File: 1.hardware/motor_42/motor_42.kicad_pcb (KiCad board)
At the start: 4 copper layers, 40 x 40 mm, 93 parts, among them IC1 TB67H450FNG,EL, IC2 TB67H450FNG,EL, J1 PC_CONN, J2 MT6816_CONN, J4 DEBUG, J5 CAN_IN, J6 CAN_OUT, J7 ESP_DOWNLOAD, J8 BOOT_EN, U1 TPS54202DDC, U2 STM32F103CBTx, U3 SN65HVD232, U4 TL431AIDBZR, U5 MT6816CT, U6 ESP32-C3-WROOM-02, Y1 YSX321SL_12Mhz

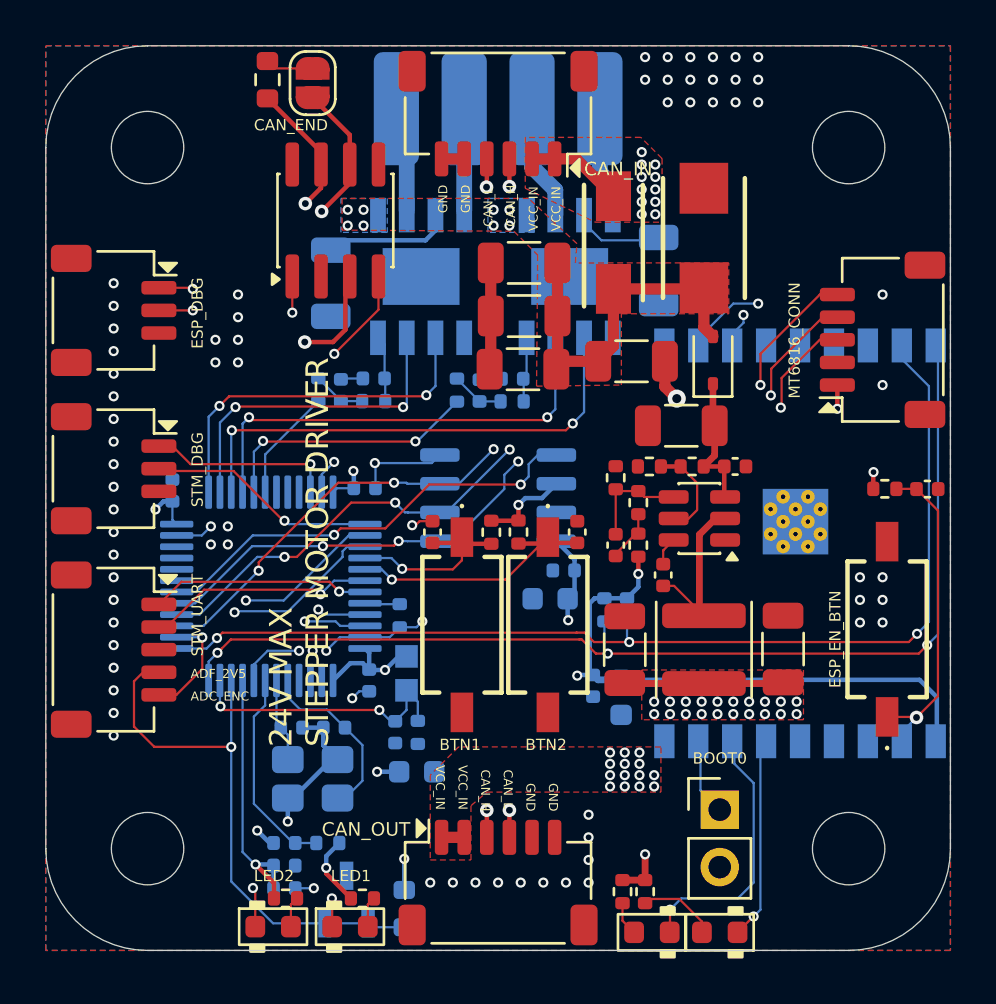
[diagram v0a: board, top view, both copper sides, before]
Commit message: 비아 변경 필요
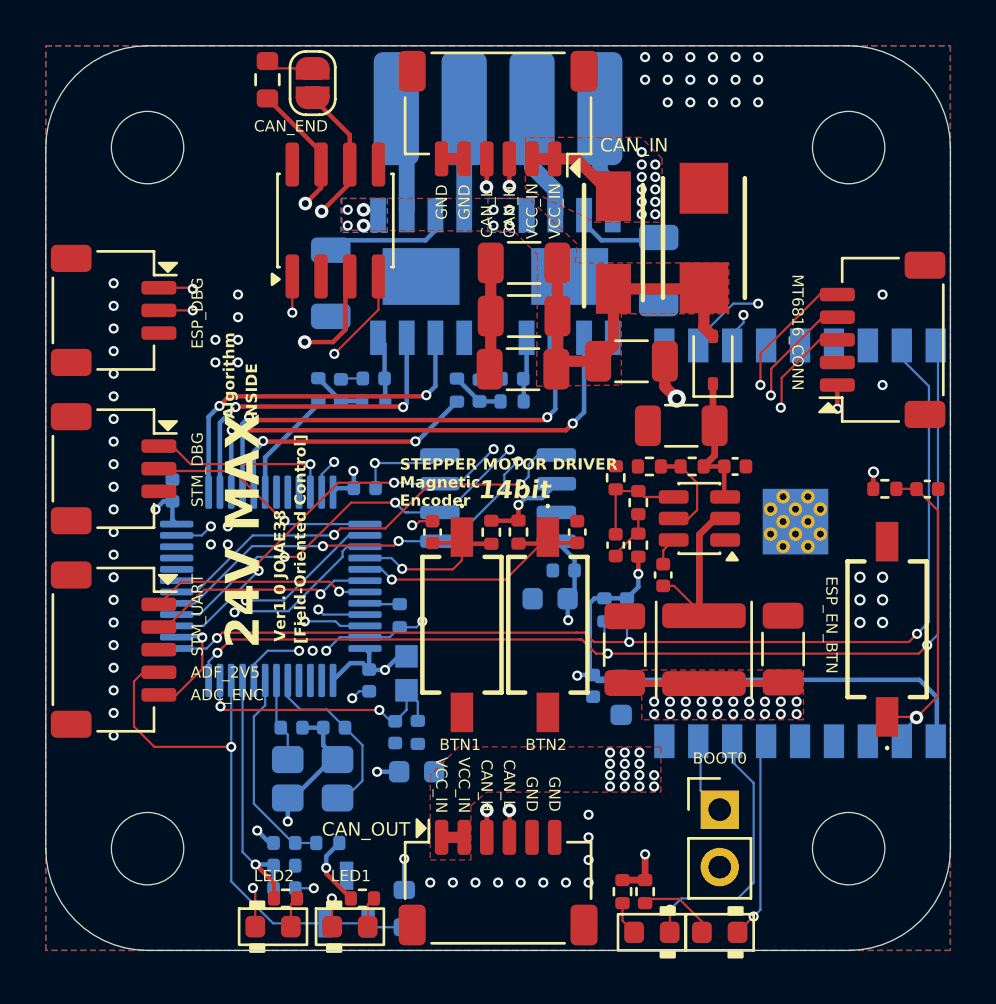
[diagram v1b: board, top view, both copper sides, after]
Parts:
- C15, C19, C31, C32: value 0.1uF/16V -> 0.1uF/50V
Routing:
- net Net-(IC1-RS): track 3.62 -> 4.12 mm
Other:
- board text added: "14bit"
- board text added: "24V MAX"
- board text added: "A-A+"
- board text added: "Algorithm"
- board text added: "B-B+"
- board text added: "INSIDE"
- board text added: "Magnetic Encoder"
- board text added: "STEPPER MOTOR DRIVER"
- board text added: "Ver1.0 JOJAE38"
- board text added: "[Field-Oriented Control]"
- board text removed: "24V MAX STEPPER MOTOR DRIVER"
- board text removed: "A+A-"
- board text removed: "B+B-"

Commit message: via 홀 0.3 직경 0.6(1.5의 폭 을 가진다) 수정 및 라우팅 개선
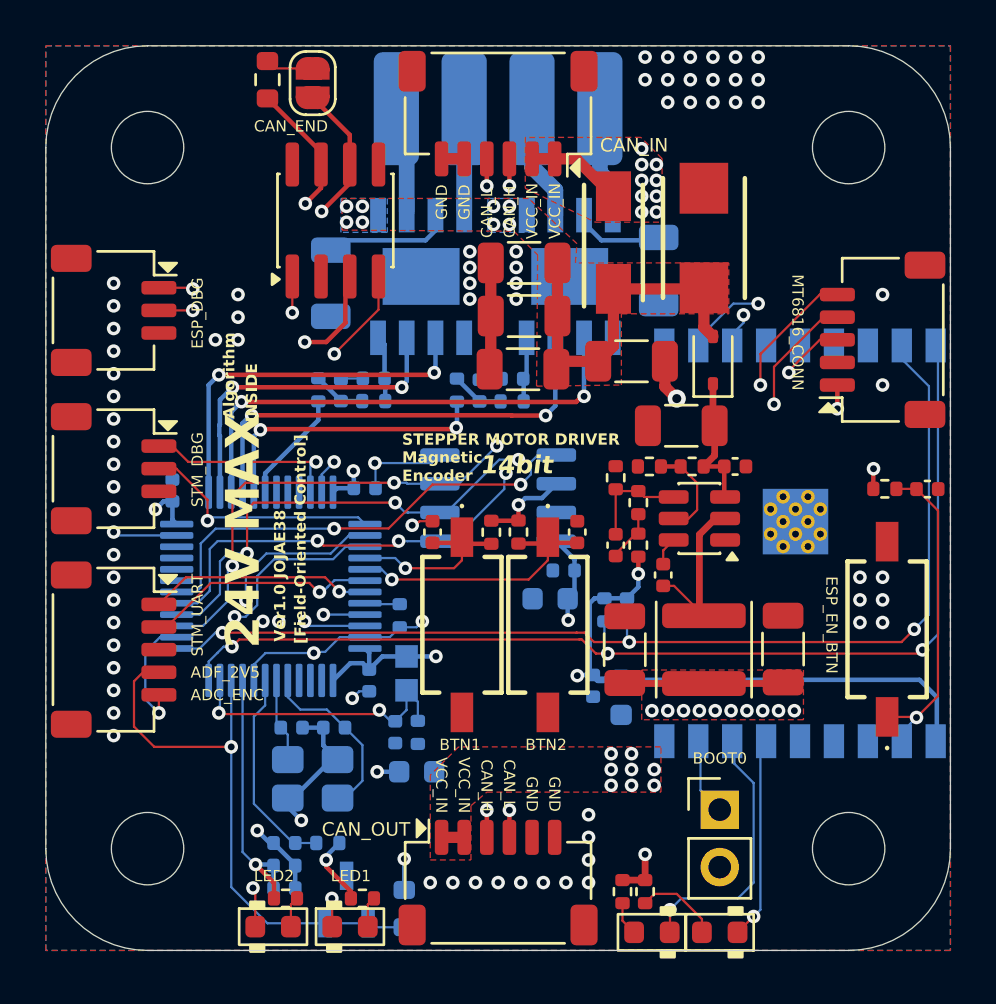
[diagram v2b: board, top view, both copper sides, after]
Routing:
- net GND: track 34.9 -> 39.1 mm, vias 79 -> 80
- net SPI1_MOSI: track 35.5 -> 37.7 mm
- net SPI1_MISO: track 36.3 -> 38.2 mm
- net 3V3: track 75.0 -> 76.2 mm, vias 35 -> 25
- net MT6816_CSN: track 19.6 -> 20.8 mm
- net VREF_PWM_A: track 11.8 -> 12.8 mm
- net SPI1_CLK: track 36.4 -> 37.3 mm
- net SWCLK: track 10.1 -> 10.9 mm
- net LED1: track 22.5 -> 23.1 mm
- net BTN2: track 11.9 -> 12.5 mm
- net LED2: track 21.4 -> 22.0 mm
- net VCC_IN: vias 25 -> 17
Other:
- board text added: "MT6816"
- board text removed: "MT6816_MAGNETIC"

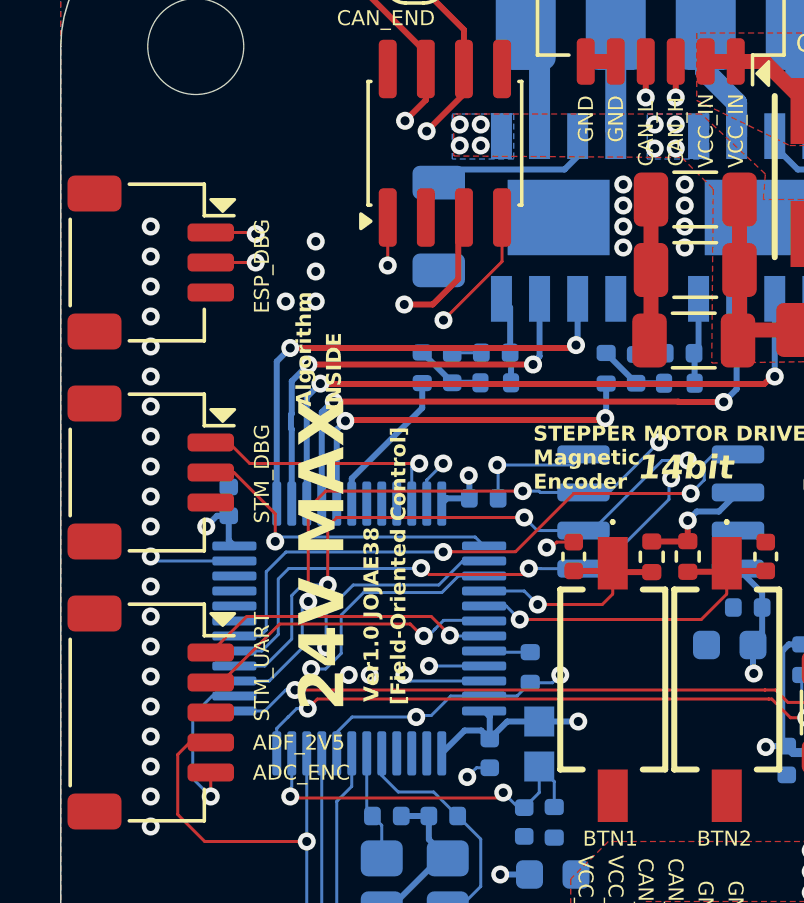
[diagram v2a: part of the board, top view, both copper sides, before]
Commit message: wifi ble 문양 추가
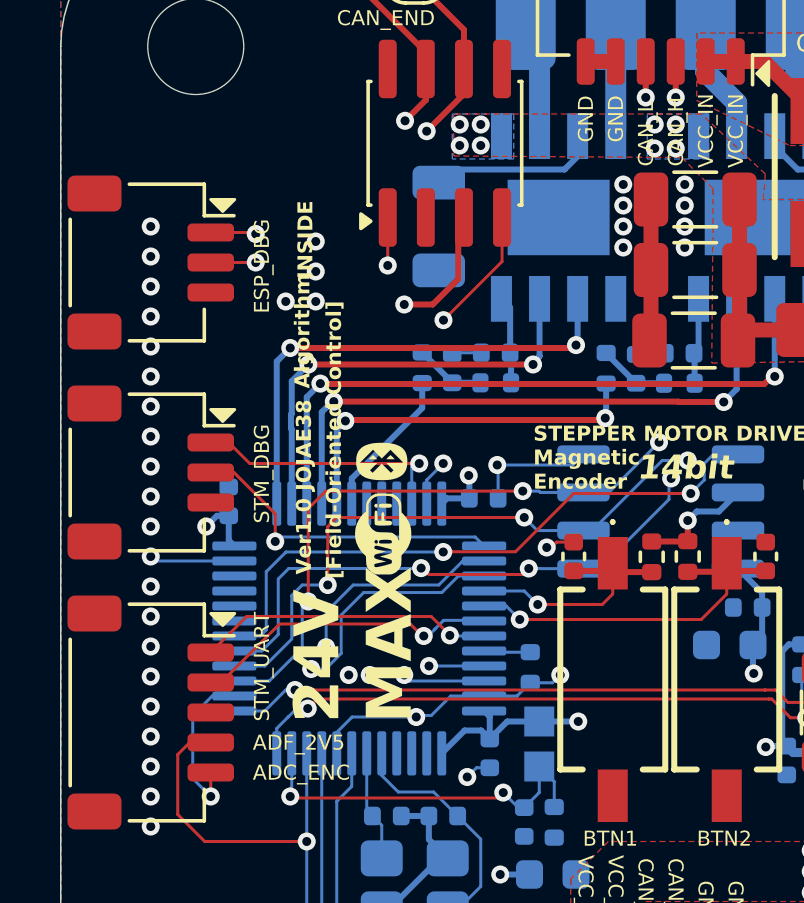
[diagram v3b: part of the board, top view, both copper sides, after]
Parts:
- added G***: LOGO, stepper_motor_controller:wifi, F.Cu at (61.8, 70.8)
- added G***: LOGO, stepper_motor_controller:ble, F.Cu at (61.7, 68.3)

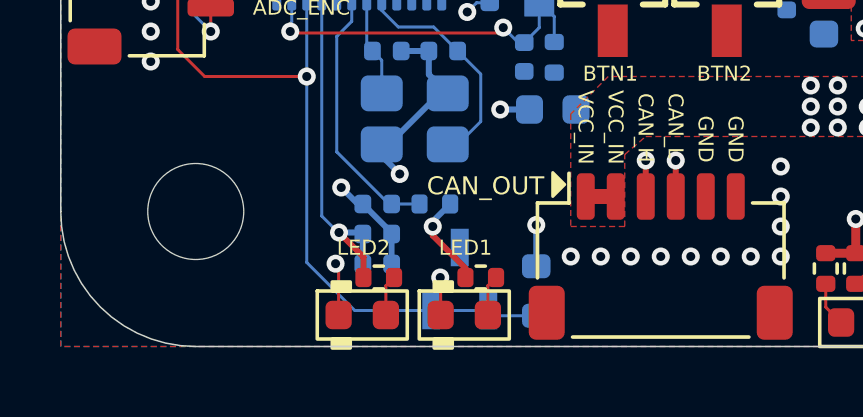
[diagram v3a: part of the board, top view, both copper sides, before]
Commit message: 번호 초기화 및 led 변경
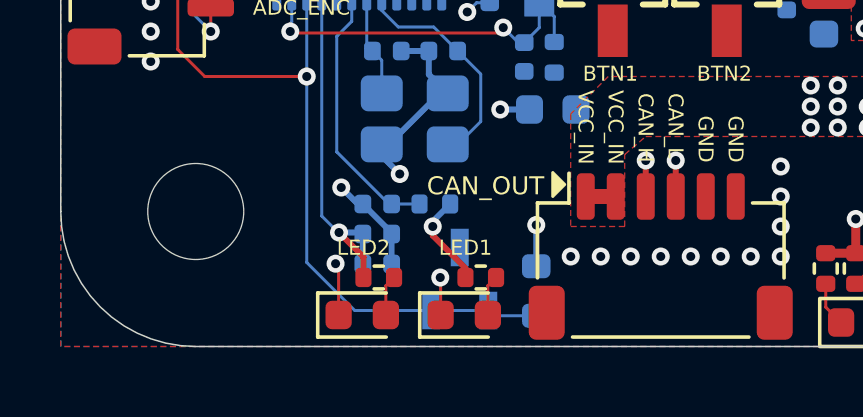
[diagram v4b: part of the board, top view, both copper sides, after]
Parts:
- removed the LED1 at (64.5, 89.0)
- removed the LED2 at (61.0, 89.0)
- added D4: Green_Led_0603, LED_SMD:LED_0603_1608Metric, F.Cu at (64.5, 89.0)
- added D5: Green_Led_0603, LED_SMD:LED_0603_1608Metric, F.Cu at (61.0, 89.0)
- C18: renamed from C36; value 1uF/10V -> 1uF/25V
- C27: renamed from C28; value 10uF/6.3V -> 10uF/10V
- C30: renamed from C33; value 2.2uF/6.3V -> 2.2uF/16V
- Y1: value YSX321SL_12Mhz -> X322512MSB4SI_12mHz
- renumbered C6 to C1, C13 to C10, C16 to C11, C17 to C12, C18 to C13, C20 to C14, C22 to C15, C23 to C16, C35 to C17, C21 to C19, C7 to C2, C14 to C20, C19 to C21, C15 to C22, C24 to C23, C25 to C24, C26 to C25, C27 to C26, C30 to C28, C32 to C29, C8 to C3, C10 to C4, C9 to C5, C2 to C6, C4 to C7, C11 to C8, C12 to C9, D4 to D1, J4 to J2, J5 to J3, J6 to J4, J7 to J5, J2 to J6, J8 to J9, L2 to L1, LED4 to LED1, LED5 to LED2, R12 to R10, R13 to R11, R11 to R12, R18 to R13, R19 to R14, R21 to R15, R22 to R16, R20 to R17, R23 to R18, R26 to R19, R6 to R2, R29 to R20, R33 to R21, R34 to R22, R28 to R23, R31 to R24, R32 to R25, R7 to R3, R2 to R4, R8 to R5, R14 to R6, R15 to R7, R10 to R8, S2 to S1, S1 to S2, U5 to U4, U4 to U5
